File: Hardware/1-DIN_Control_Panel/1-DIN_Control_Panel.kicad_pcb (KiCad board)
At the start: 2 copper layers, 177.8 x 255.2 mm, 83 parts, among them J1 Selector Knob Connector, J2 Rotary Switch 1x7, J3 2x05 Molex Micro-Fit 3.0 43045, J4 UART Expansion, J5 SW - Aux Jump-Start, J6 SW - Battery Bypass, J7 SW - Master Power, J8 Pot/SW - Brightness, K1 FINDER-40.52, U1 CA56-12SEKWA, U2 CA56-12SEKWA, U3 LTV-847S, U4 LTV-847S, U5 MAX 6954 - SSOP, U6 MAX 6954 - SSOP, U7 LM324DR, U8 12V->5V Variable Boost Buck C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

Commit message: Organized schematic into two pages, begun PCB routing
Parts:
- removed C16, C17: DNP, Capacitor_SMD:C_0603_1608Metric_Pad1.08x0.95mm_HandSolder
- removed C18: 22µF, Capacitor_SMD:C_0603_1608Metric_Pad1.08x0.95mm_HandSolder
- removed R21: 0Ω or Bridge, Resistor_SMD:R_0603_1608Metric_Pad0.98x0.95mm_HandSolder
- removed TP10, TP11, TP12, TP13, TP14, TP3, TP4, TP5, TP6, TP7, TP8, TP9: TestPoint_Flag, TestPoint:TestPoint_Loop_D2.54mm_Drill1.5mm_Beaded
- added J10: 2x05 Molex Micro-Fit 3.0 43045, libraries:MOLEX_430450615, F.Cu at (169.4, 51.2)
- added J11: 2x05 Molex Micro-Fit 3.0 43045, libraries:MOLEX_430450615, B.Cu at (179.2, 151.8)
- added J12: Display LEDs, Connector_Molex:Molex_Micro-Fit_3.0_43045-0812_2x04_P3.00mm_Vertical, B.Cu at (91.2, 113.4)
- added J13: Mode LEDs, Connector_Molex:Molex_Micro-Fit_3.0_43045-0812_2x04_P3.00mm_Vertical, F.Cu at (82.2, 44.0)
- added J9: 2x05 Molex Micro-Fit 3.0 43045, libraries:MOLEX_430450615, B.Cu at (179.3, 123.1)
- added U10: XZFAVG10, libraries:XZFAVG10, F.Cu at (167.9, 147.1)
- added U11: MAX 6954 - SSOP, libraries:MAX6954-SSOP, B.Cu at (154.0, 134.8)
- added U12: LM324DR, Package_SO:SOIC-14_3.9x8.7mm_P1.27mm, F.Cu at (134.0, 64.2)
- added U13: 12V->5V Variable Boost Buck Converter, libraries:BoostBuck, F.Cu at (35.2, 87.2)
- added U9: XZFAVG10, libraries:XZFAVG10, F.Cu at (158.7, 147.1)
- A1: footprint Module:Arduino_Nano -> Module:Arduino_Nano_WithMountingHoles
- C1: value 47µF -> 22pF
- C11: value 100nF -> 10µF
- C12, C13: value 100nF -> DNP
- C14: value 100nF -> 22µF
- C15: value 10µF -> 100nF
- C2: footprint Capacitor_SMD:C_0603_1608Metric_Pad1.08x0.95mm_HandSolder -> Capacitor_SMD:C_1206_3216Metric_Pad1.33x1.80mm_HandSolder
- C7, C8: value 22pF -> 100nF
- J1: footprint libraries:Mystery_RJ45 -> Connector_Molex:Molex_Micro-Fit_3.0_43045-0812_2x04_P3.00mm_Vertical; moved to B.Cu
- J3, J4, R2, R3, R4, R5, R6, R7, R8: moved to B.Cu
- J8: footprint TerminalBlock:TerminalBlock_bornier-5_P5.08mm -> Connector_Molex:Molex_Micro-Fit_3.0_43650-0515_1x05_P3.00mm_Vertical
- R9: value 56kΩ -> 0Ω or Bridge
- RV1: footprint Buzzer_Beeper:Buzzer_12x9.5RM7.6 -> Potentiometer_THT:Potentiometer_Runtron_RM-065_Vertical
- TP1, TP2: footprint TestPoint:TestPoint_Loop_D2.54mm_Drill1.5mm_Beaded -> TestPoint:TestPoint_Pad_D4.0mm
- U1, U2: value CA56-12SEKWA -> XZFAVG10; footprint Display_7Segment:CA56-12SEKWA -> libraries:XZFAVG10
- U3, U4: value LTV-847S -> XZFAVG10; footprint Package_DIP:SMDIP-16_W9.53mm -> libraries:XZFAVG10
- U5, U6: value MAX 6954 - SSOP -> LTV-847S; footprint Package_SO:SSOP-44_5.3x12.8mm_P0.5mm -> Package_DIP:SMDIP-16_W9.53mm
- U7: value LM324DR -> XZFAVG10; footprint Package_SO:SOIC-14_3.9x8.7mm_P1.27mm -> libraries:XZFAVG10
- U8: value 12V->5V Variable Boost Buck Converter -> XZFAVG10; footprint libraries:BoostBuck -> libraries:XZFAVG10
- moved TP2 157.3 mm to (207.3, 149.4)
- moved TP1 157.0 mm to (207.3, 143.4)
- moved J4 149.3 mm to (181.1, 71.4), turned to -90 degrees
- moved J8 143.5 mm to (174.0, 85.2)
- moved U8 141.4 mm to (149.3, 147.1)
- moved C1 135.8 mm to (200.3, 134.7)
- moved U1 134.0 mm to (140.1, 122.8)
- moved C2 133.1 mm to (204.3, 126.5)
- moved C3 128.5 mm to (199.1, 128.6)
- moved C6 125.9 mm to (199.1, 131.2)
- moved U3 125.4 mm to (158.7, 122.8)
- moved U2 124.7 mm to (149.3, 122.8)
- moved U4 121.5 mm to (167.9, 122.8)
- moved R10 120.4 mm to (200.6, 137.3)
- moved C8 119.8 mm to (208.1, 48.8)
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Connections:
- net /12V_ON renamed /Back Board/12V_ON
- net /BATT_BYPASS renamed /Back Board/BATT_BYPASS
- net /BATT_RAW renamed /Back Board/BATT_RAW
- net /CONTACTOR_COIL renamed /Back Board/CONTACTOR_COIL
- net /MASTER_COMMON renamed /Back Board/MASTER_COMMON
- net /MASTER_OPEN renamed /Back Board/MASTER_OPEN
- net /RX-EXPANSION renamed /Back Board/RX-EXPANSION
- net /TX-EXPANSION renamed /Back Board/TX-EXPANSION
- net /VOLT_SOURCE_SELECT renamed /Back Board/VOLT_SOURCE_SELECT
- A1 pad 12: /Arduino_~{CS}_VOLT -> unconnected-(A1-D9-Pad12)
- A1 pad 13: /Arduino_~{CS}_AMP -> /Back Board/Arduino_~{CS}
- A1 pad 14: /Arduino_MOSI -> /Back Board/Arduino_MOSI
- A1 pad 15: /Arduino_MISO -> /Back Board/Arduino_MISO
- A1 pad 16: /Arduino_SCK -> /Back Board/Arduino_SCK
- A1 pad 19: /BRIGHTNESS_CONTROL -> /Back Board/BRIGHTNESS_CONTROL
- A1 pad 20: /VOLTAGE_SENSE -> /Back Board/VOLTAGE_SENSE
- A1 pad 21: /CURRENT_SENSE -> /Back Board/CURRENT_SENSE
- A1 pad 6: /MODE_LED_BRIGHTNESS -> /Back Board/MODE_LED_BRIGHTNESS
- A1 pad 7: /MODE_PWR_DETECT -> /Back Board/MODE_PWR_DETECT
- C1 pad 1: Net-(C1-Pad1) -> Net-(U11-OSC)
- C10 pad 1: /BRIGHTNESS_CONTROL -> /Back Board/SHUNT-
- C11 pad 1: /CURRENT_SENSE -> VCC
- C12 pad 1: /VOLTAGE_SENSE -> Net-(U12A--)
- C13 pad 1: /SHUNT+ -> Net-(U12A-+)
- C14 pad 1: /SHUNT- -> +5V
- C15 pad 1: VCC -> +5V
- C2 pad 1: Net-(C2-Pad1) -> +5V
- C3 pad 1: Net-(C1-Pad1) -> +5V
- C4 pad 1: Net-(C2-Pad1) -> /Back Board/VOLTAGE_SENSE
- C5 pad 1: Net-(C1-Pad1) -> /Back Board/BRIGHTNESS_CONTROL
- C6 pad 1: Net-(C2-Pad1) -> +5V
- C7 pad 1: Net-(U5-OSC) -> /Back Board/CURRENT_SENSE
- C8 pad 1: Net-(U6-OSC) -> /Back Board/VOLTAGE_SENSE
- C9 pad 1: /VOLTAGE_SENSE -> /Back Board/SHUNT+
- D1 pad 1: /MODE_1_LED -> Net-(D1-K)
- D2 pad 1: /MODE_2_LED -> Net-(D1-K)
- D3 pad 1: /MODE_3_LED -> Net-(D1-K)
- D4 pad 1: /MODE_4_LED -> Net-(D1-K)
- D5 pad 1: /MODE_5_LED -> Net-(D1-K)
- D6 pad 1: /MODE_6_LED -> Net-(D1-K)
- D7 pad 1: /MODE_7_LED -> Net-(D1-K)
- D9 pad 2: /SHUNT+ -> /Back Board/SHUNT+
- J1 pad 1: /MODE_1_OUT -> /Back Board/MODE_12V_OUT
- J1 pad 2: /MODE_2_OUT -> /Back Board/MODE_7_OUT
- J1 pad 3: /MODE_3_OUT -> /Back Board/MODE_6_OUT
- J1 pad 4: /MODE_4_OUT -> /Back Board/MODE_5_OUT
- J1 pad 5: /MODE_5_OUT -> /Back Board/MODE_4_OUT
- J1 pad 6: /MODE_6_OUT -> /Back Board/MODE_3_OUT
- J1 pad 7: /MODE_7_OUT -> /Back Board/MODE_2_OUT
- J1 pad 8: /MODE_12V_OUT -> /Back Board/MODE_1_OUT
- J2 pad 1: /MODE_1 -> /Back Board/MODE_1
- J2 pad 2: /MODE_2 -> /Back Board/MODE_2
- J2 pad 3: /MODE_3 -> /Back Board/MODE_3
- J2 pad 4: /MODE_4 -> /Back Board/MODE_4
- J2 pad 5: /MODE_5 -> /Back Board/MODE_5
- J2 pad 6: /MODE_6 -> /Back Board/MODE_6
- J2 pad 7: /MODE_7 -> /Back Board/MODE_7
- J2 pad 8: /MODE_12V -> /Back Board/MODE_12V
- J3 pad 2: /SHUNT+ -> /Back Board/SHUNT+
- J3 pad 3: /SHUNT- -> /Back Board/SHUNT-
- J6 pad 1: /SHUNT+ -> /Back Board/SHUNT+
- J8 pad 2: /BRIGHTNESS_CONTROL -> /Back Board/BRIGHTNESS_CONTROL
- R1 pad 2: /MODE_PWR_DETECT -> /Back Board/MODE_PWR_DETECT
- R10 pad 2: Net-(U6-ISET) -> Net-(U11-ISET)
- R12 pad 1: /VOLTAGE_SENSE -> /Back Board/VOLTAGE_SENSE
- R13 pad 2: /VOLTAGE_SENSE -> /Back Board/VOLTAGE_SENSE
- R14 pad 1: Net-(U7B--) -> Net-(U12B--)
- R15 pad 2: Net-(U7B--) -> Net-(U12B--)
- R16 pad 2: Net-(U7C--) -> Net-(U12C--)
- R17 pad 2: Net-(U7A--) -> Net-(U12A--)
- R18 pad 2: Net-(U7A-+) -> Net-(U12A-+)
- R19 pad 1: Net-(U7A--) -> Net-(U12A--)
- R19 pad 2: /CURRENT_SENSE -> /Back Board/CURRENT_SENSE
- R2 pad 1: Net-(R2-Pad1) -> Net-(J12-Pin_1)
- R20 pad 1: Net-(U7A-+) -> Net-(U12A-+)
- R3 pad 1: Net-(R2-Pad1) -> Net-(J12-Pin_2)
- R4 pad 1: Net-(R2-Pad1) -> Net-(J12-Pin_3)
- R5 pad 1: Net-(R2-Pad1) -> Net-(J12-Pin_4)
- R6 pad 1: Net-(R2-Pad1) -> Net-(J12-Pin_5)
- R7 pad 1: Net-(R2-Pad1) -> Net-(J12-Pin_6)
- R8 pad 1: Net-(R2-Pad1) -> Net-(J12-Pin_7)
- R9 pad 1: GND -> /Back Board/MODE_LED_BRIGHTNESS
- R9 pad 2: Net-(U5-ISET) -> Net-(J13-Pin_8)
- RV1 pad 2: Net-(U7C--) -> Net-(U12C--)
- TP1 pad 1: Net-(U5-P0) -> Net-(U11-BLINK)
- TP2 pad 1: Net-(U5-P1) -> Net-(U11-OSC_OUT)
- U1 pad 1: /DIGIT1_G2-N_ANODE -> /Front Board/6954_O10
- U1 pad 10: /DIGIT3_G2-N_ANODE -> /Front Board/6954_O2
- U1 pad 11: /DIGIT3_A-G1_ANODE -> /Front Board/6954_O4
- U1 pad 12: /F_CATHODE -> /Front Board/6954_O11
- U1 pad 2: /DIGIT2_G2-N_ANODE -> /Front Board/6954_O17
- U1 pad 3: /D_CATHODE -> /Front Board/6954_O13
- U1 pad 4: /C_CATHODE -> /Front Board/6954_O16
- U1 pad 5: /G_CATHODE -> /Front Board/6954_O18
- U1 pad 6: /E_CATHODE -> /Front Board/6954_O5
- U1 pad 7: /COLON_DP_ANODE -> /Front Board/6954_O6
- U1 pad 8: /DIGIT4_A-G1_ANODE -> /Front Board/6954_O8
- U1 pad 9: /DIGIT4_G2-N_ANODE -> /Front Board/6954_O14
- U2 pad 1: /DIGIT1_G2-N_ANODE -> /Front Board/6954_O10
- U2 pad 10: /DIGIT3_G2-N_ANODE -> /Front Board/6954_O0
- U2 pad 11: /DIGIT3_A-G1_ANODE -> /Front Board/6954_O2
- U2 pad 12: /F_CATHODE -> /Front Board/6954_O11
- U2 pad 2: /DIGIT2_G2-N_ANODE -> /Front Board/6954_O17
- U2 pad 3: /D_CATHODE -> /Front Board/6954_O13
- U2 pad 4: /C_CATHODE -> /Front Board/6954_O16
- U2 pad 5: /G_CATHODE -> /Front Board/6954_O18
- U2 pad 6: /E_CATHODE -> /Front Board/6954_O3
- U2 pad 7: /COLON_DP_ANODE -> /Front Board/6954_O6
- U2 pad 8: /DIGIT4_A-G1_ANODE -> /Front Board/6954_O8
- U2 pad 9: /DIGIT4_G2-N_ANODE -> /Front Board/6954_O14
- U3 pad 1: /MODE_1 -> /Front Board/6954_O10
- U3 pad 10: /MODE_4_LED -> /Front Board/6954_O2
- U3 pad 11: GND -> /Front Board/6954_O4
- U3 pad 12: /MODE_3_LED -> /Front Board/6954_O11
- U3 pad 13: GND -> /Front Board/6954_O15
- U3 pad 14: /MODE_2_LED -> /Front Board/6954_O1
- U3 pad 15: GND -> /Front Board/6954_O12
- U3 pad 16: /MODE_1_LED -> /Front Board/6954_O9
- U3 pad 2: /MODE_1_OUT -> /Front Board/6954_O17
- U3 pad 3: /MODE_2 -> /Front Board/6954_O13
- U3 pad 4: /MODE_2_OUT -> /Front Board/6954_O16
- U3 pad 5: /MODE_3 -> /Front Board/6954_O18
- U3 pad 6: /MODE_3_OUT -> /Front Board/6954_O5
- U3 pad 7: /MODE_4 -> /Front Board/6954_O6
- U3 pad 8: /MODE_4_OUT -> /Front Board/6954_O8
- U3 pad 9: GND -> /Front Board/6954_O14
- U4 pad 1: /MODE_5 -> /Front Board/6954_O10
- U4 pad 10: +5V -> /Front Board/6954_O0
- U4 pad 11: GND -> /Front Board/6954_O2
- U4 pad 12: /MODE_7_LED -> /Front Board/6954_O11
- U4 pad 13: GND -> /Front Board/6954_O15
- U4 pad 14: /MODE_6_LED -> /Front Board/6954_O5
- U4 pad 15: GND -> /Front Board/6954_O12
- U4 pad 16: /MODE_5_LED -> /Front Board/6954_O9
- U4 pad 2: /MODE_5_OUT -> /Front Board/6954_O17
- U4 pad 3: /MODE_6 -> /Front Board/6954_O13
- U4 pad 4: /MODE_6_OUT -> /Front Board/6954_O16
- U4 pad 5: /MODE_7 -> /Front Board/6954_O18
- U4 pad 6: /MODE_7_OUT -> /Front Board/6954_O3
- U4 pad 7: /MODE_12V_OUT -> /Front Board/6954_O6
- U4 pad 8: /MODE_12V -> /Front Board/6954_O8
- U4 pad 9: /MODE_PWR_DETECT -> /Front Board/6954_O14
- U5 pad 1: Net-(U5-P0) -> /Back Board/MODE_1
- U5 pad 10: /DIGIT2_G2-N_ANODE -> /Back Board/MODE_4_LED
- U5 pad 11: /DIGIT3_A-G1_ANODE -> GND
- U5 pad 12: /DIGIT3_G2-N_ANODE -> /Back Board/MODE_3_LED
- U5 pad 13: /DIGIT4_A-G1_ANODE -> GND
- U5 pad 14: /DIGIT4_G2-N_ANODE -> /Back Board/MODE_2_LED
- U5 pad 15: /COLON_DP_ANODE -> GND
- U5 pad 16: GND -> /Back Board/MODE_1_LED
- U5 pad 2: Net-(U5-P1) -> /Back Board/MODE_1_OUT
- U5 pad 3: /Arduino_~{CS}_VOLT -> /Back Board/MODE_2
- U5 pad 4: /Arduino_MISO -> /Back Board/MODE_2_OUT
- U5 pad 5: /Arduino_SCK -> /Back Board/MODE_3
- U5 pad 6: /Arduino_MOSI -> /Back Board/MODE_3_OUT
- U5 pad 7: /DIGIT1_A-G1_ANODE -> /Back Board/MODE_4
- U5 pad 8: /DIGIT1_G2-N_ANODE -> /Back Board/MODE_4_OUT
- U5 pad 9: /DIGIT2_A-G1_ANODE -> GND
- U6 pad 1: Net-(U6-P0) -> /Back Board/MODE_5
- U6 pad 10: /DIGIT2_G2-N_ANODE -> +5V
- U6 pad 11: /DIGIT3_A-G1_ANODE -> GND
- U6 pad 12: /DIGIT3_G2-N_ANODE -> /Back Board/MODE_7_LED
- U6 pad 13: /DIGIT4_A-G1_ANODE -> GND
- U6 pad 14: /DIGIT4_G2-N_ANODE -> /Back Board/MODE_6_LED
- U6 pad 15: /COLON_DP_ANODE -> GND
- U6 pad 16: GND -> /Back Board/MODE_5_LED
- U6 pad 2: Net-(U6-P1) -> /Back Board/MODE_5_OUT
- U6 pad 3: /Arduino_~{CS}_AMP -> /Back Board/MODE_6
- U6 pad 4: /Arduino_MISO -> /Back Board/MODE_6_OUT
- U6 pad 5: /Arduino_SCK -> /Back Board/MODE_7
- U6 pad 6: /Arduino_MOSI -> /Back Board/MODE_7_OUT
- U6 pad 7: /DIGIT1_A-G1_ANODE -> /Back Board/MODE_12V_OUT
- U6 pad 8: /DIGIT1_G2-N_ANODE -> /Back Board/MODE_12V
- U6 pad 9: /DIGIT2_A-G1_ANODE -> /Back Board/MODE_PWR_DETECT
- U7 pad 1: /CURRENT_SENSE -> /Front Board/6954_O10
- U7 pad 10: /SHUNT- -> /Front Board/6954_O0
- U7 pad 11: GND -> /Front Board/6954_O4
- U7 pad 12: unconnected-(U7D-+-Pad12) -> /Front Board/6954_O11
- U7 pad 13: unconnected-(U7D---Pad13) -> /Front Board/6954_O15
- U7 pad 14: unconnected-(U7-Pad14) -> /Front Board/6954_O2
- U7 pad 2: Net-(U7A--) -> /Front Board/6954_O17
- U7 pad 3: Net-(U7A-+) -> /Front Board/6954_O13
- U7 pad 4: +5V -> /Front Board/6954_O16
- U7 pad 5: /SHUNT+ -> /Front Board/6954_O18
- U7 pad 6: Net-(U7B--) -> /Front Board/6954_O5
- U7 pad 7: Net-(R14-Pad2) -> /Front Board/6954_O6
- U7 pad 8: Net-(R16-Pad1) -> /Front Board/6954_O8
- U7 pad 9: Net-(U7C--) -> /Front Board/6954_O14
- U8 pad 1: VCC -> /Front Board/6954_O10
- U8 pad 2: GND -> /Front Board/6954_O17
- U8 pad 3: +5V -> /Front Board/6954_O13
- U8 pad 4: GND -> /Front Board/6954_O16
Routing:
- net Net-(D1-K): track 0.00 -> 88.3 mm
- net Net-(D7-A): track 0.00 -> 41.6 mm, vias 0 -> 1
- net Net-(D1-A): track 0.00 -> 33.4 mm, vias 0 -> 1
- net Net-(J12-Pin_5): track 0.00 -> 32.8 mm
- net Net-(J12-Pin_1): track 0.00 -> 32.8 mm
- net Net-(D6-A): track 0.00 -> 31.1 mm, vias 0 -> 1
- net Net-(D2-A): track 0.00 -> 28.2 mm, vias 0 -> 1
- net Net-(J12-Pin_2): track 0.00 -> 25.3 mm
- net Net-(J12-Pin_6): track 0.00 -> 24.9 mm
- net Net-(D5-A): track 0.00 -> 21.5 mm, vias 0 -> 1
- net Net-(R14-Pad2): track 0.00 -> 18.5 mm, vias 0 -> 2
- net Net-(R15-Pad1): track 0.00 -> 18.1 mm, vias 0 -> 2
- net Net-(J12-Pin_3): track 0.00 -> 17.4 mm
- net Net-(D3-A): track 0.00 -> 15.3 mm, vias 0 -> 1
- net Net-(J12-Pin_7): track 0.00 -> 14.3 mm
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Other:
- board size 177.8 x 255.2 mm -> 374.9 x 296.6 mm

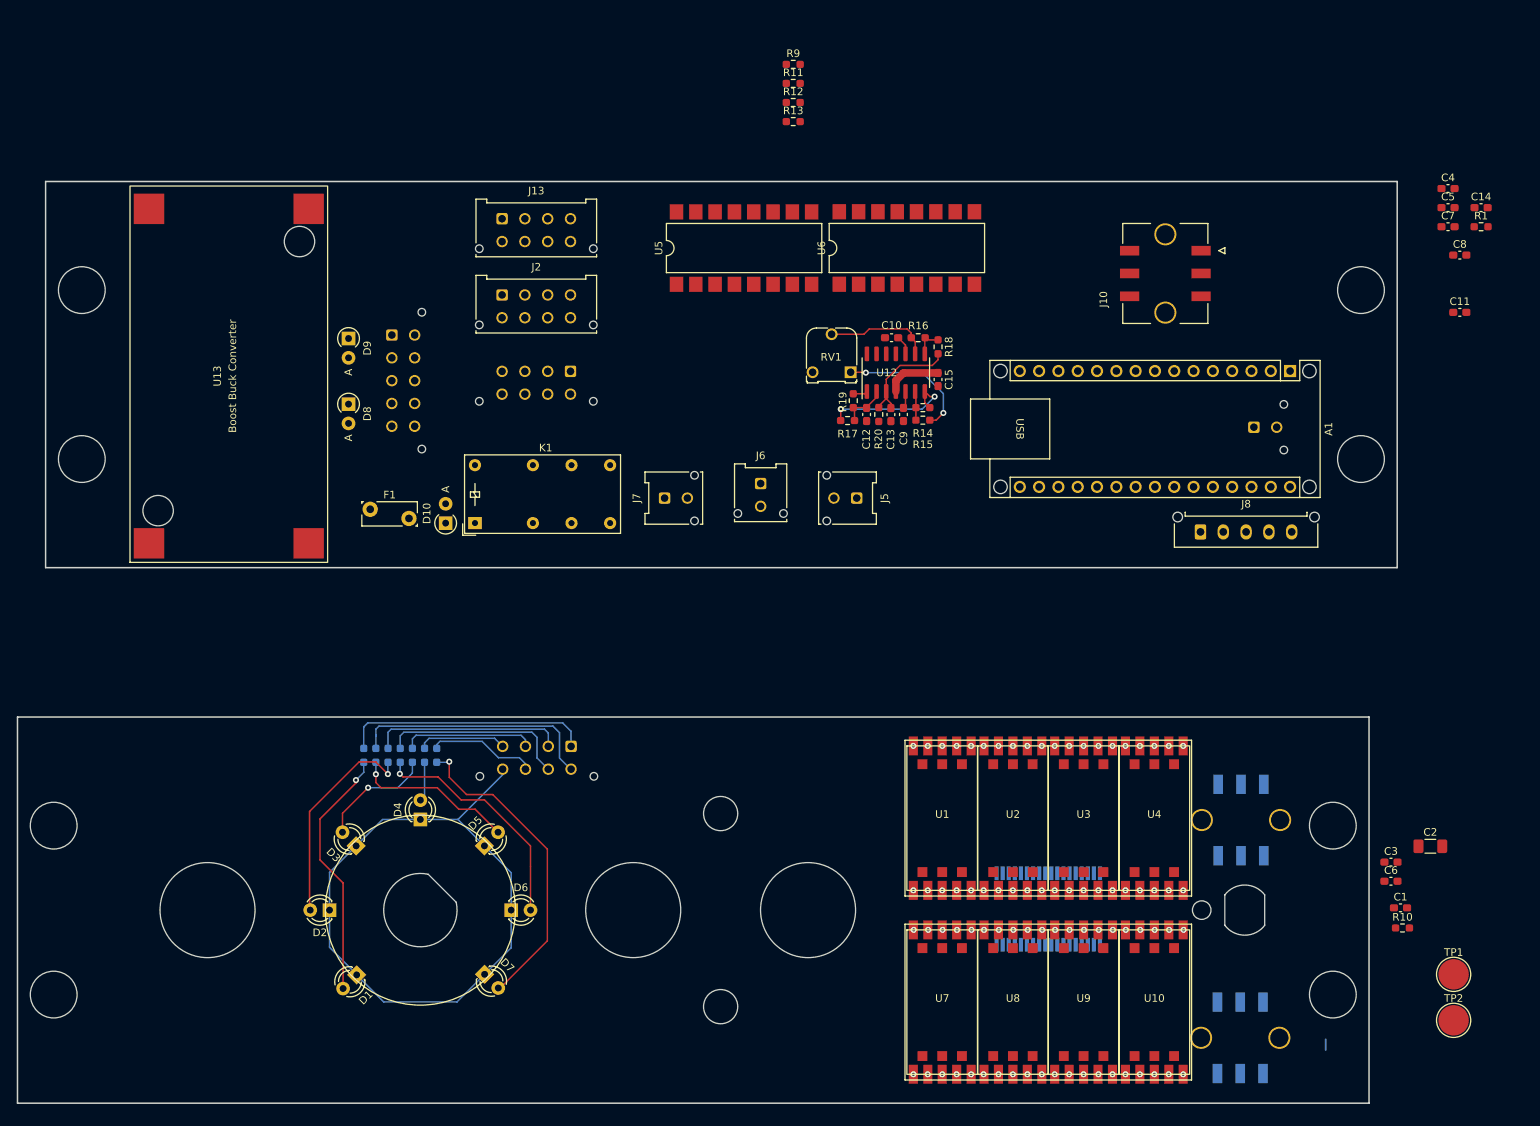
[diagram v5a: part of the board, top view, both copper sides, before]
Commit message: Finished routing of rear board
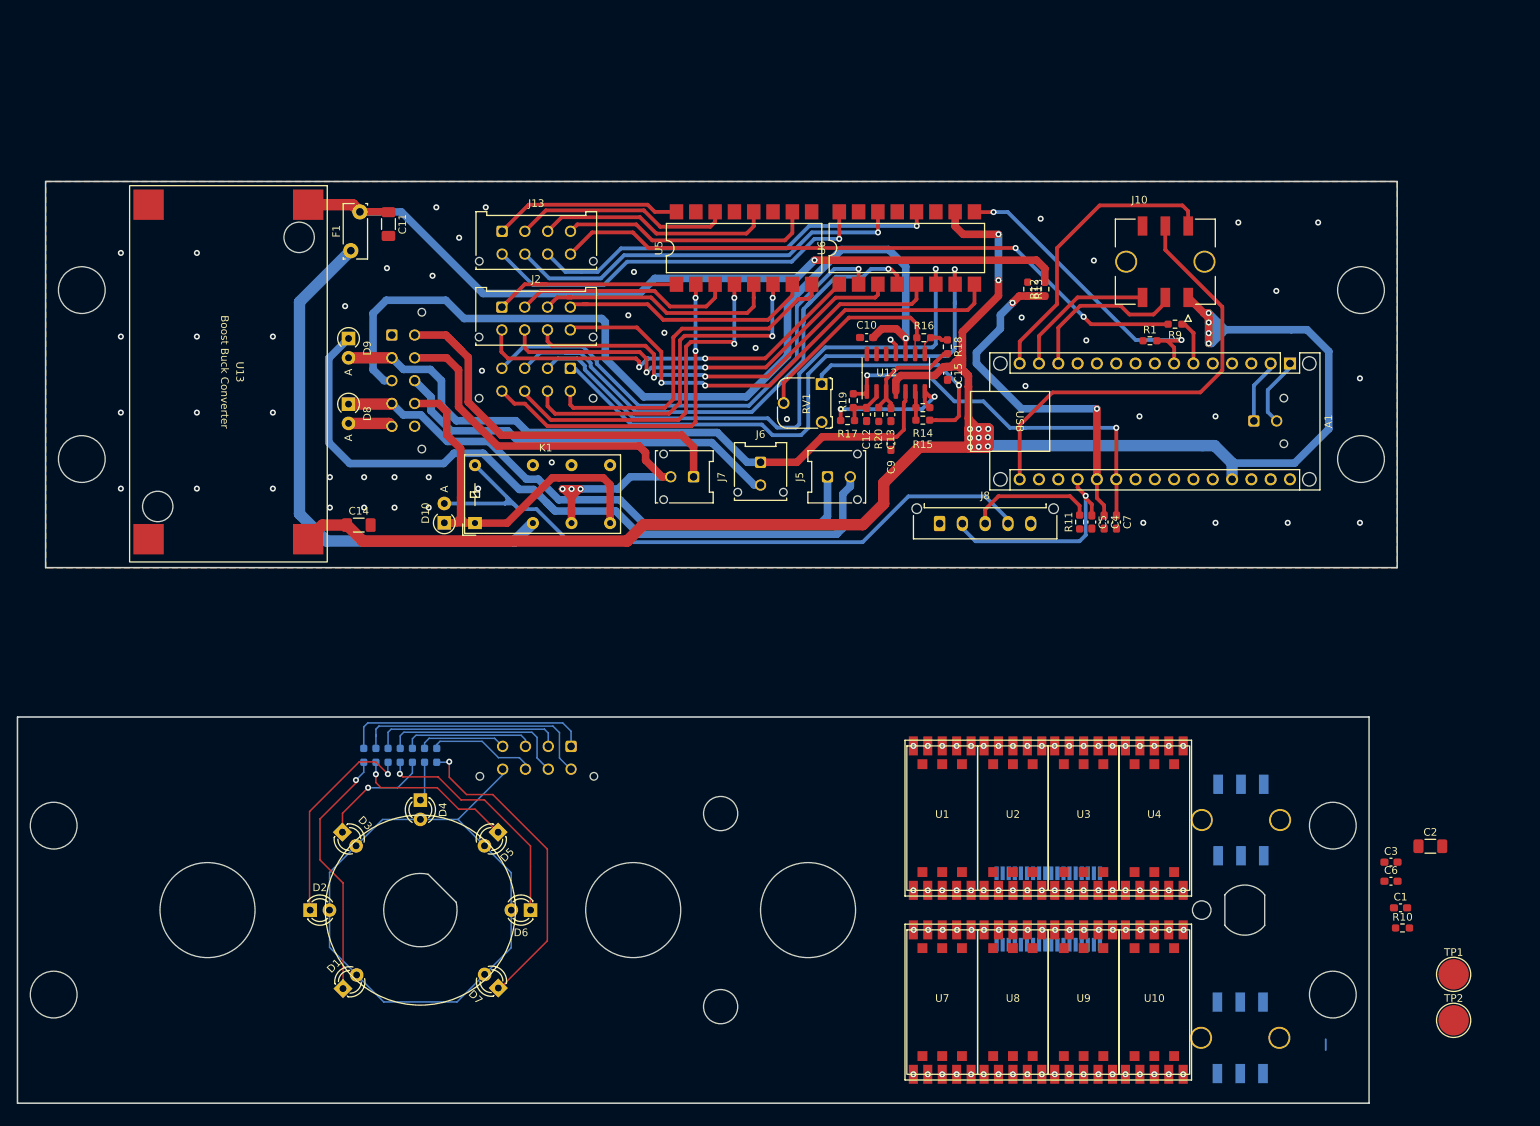
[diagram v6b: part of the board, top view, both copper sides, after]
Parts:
- removed C8: 100nF, Capacitor_SMD:C_0603_1608Metric_Pad1.08x0.95mm_HandSolder
- C11, C14: footprint Capacitor_SMD:C_0603_1608Metric_Pad1.08x0.95mm_HandSolder -> Capacitor_SMD:C_1206_3216Metric_Pad1.33x1.80mm_HandSolder
- moved C14 153.4 mm to (63.3, 84.3)
- moved C11 141.4 mm to (67.2, 44.7), turned to -90 degrees
- moved R11 68.9 mm to (158.1, 83.9), turned to 90 degrees
- moved C4 63.0 mm to (161.3, 83.9), turned to -90 degrees
- moved C5 62.5 mm to (159.7, 83.9), turned to -90 degrees
- moved R9 60.8 mm to (170.7, 57.9), turned to 180 degrees
- moved C7 58.4 mm to (163.0, 83.9), turned to -90 degrees
- moved U13 50.6 mm to (57.2, 41.6), turned to -90 degrees
- moved R1 46.1 mm to (167.4, 60.0)
- moved R12 41.2 mm to (153.6, 53.3), turned to 90 degrees
- moved R13 37.9 mm to (151.3, 53.3), turned to -90 degrees
- moved J8 34.3 mm to (139.7, 84.1)
- moved F1 34.1 mm to (62.2, 48.2), turned to 90 degrees
- moved J5 4.75 mm to (125.0, 77.9), turned to 90 degrees
- moved J7 4.73 mm to (107.3, 78.0), turned to -90 degrees
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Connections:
- D2 pad 1: Net-(D1-K) -> Net-(D2-K)
- D2 pad 2: Net-(D2-A) -> Net-(D1-A)
- D3 pad 1: Net-(D1-K) -> Net-(D3-K)
- D3 pad 2: Net-(D3-A) -> Net-(D1-A)
- D4 pad 1: Net-(D1-K) -> Net-(D4-K)
- D4 pad 2: Net-(D4-A) -> Net-(D1-A)
- D5 pad 1: Net-(D1-K) -> Net-(D5-K)
- D5 pad 2: Net-(D5-A) -> Net-(D1-A)
- D6 pad 1: Net-(D1-K) -> Net-(D6-K)
- D6 pad 2: Net-(D6-A) -> Net-(D1-A)
- D7 pad 1: Net-(D1-K) -> Net-(D7-K)
- D7 pad 2: Net-(D7-A) -> Net-(D1-A)
- J12 pad 8: Net-(D1-K) -> Net-(D1-A)
- R2 pad 2: Net-(D1-A) -> Net-(D1-K)
- R3 pad 2: Net-(D2-A) -> Net-(D2-K)
- R4 pad 2: Net-(D3-A) -> Net-(D3-K)
- R5 pad 2: Net-(D4-A) -> Net-(D4-K)
- R6 pad 2: Net-(D5-A) -> Net-(D5-K)
- R7 pad 2: Net-(D6-A) -> Net-(D6-K)
- R8 pad 2: Net-(D7-A) -> Net-(D7-K)
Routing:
- net +5V: track 7.40 -> 289.5 mm, vias 0 -> 15
- net /Back Board/SHUNT-: track 2.53 -> 119.1 mm, vias 0 -> 1
- net VCC: track 0.00 -> 109.1 mm, vias 0 -> 1
- net Net-(D9-K): track 0.00 -> 97.2 mm
- net /Back Board/VOLT_SOURCE_SELECT: track 0.00 -> 90.5 mm
- net /Back Board/SHUNT+: track 2.27 -> 87.6 mm
- net Net-(J13-Pin_8): track 0.00 -> 84.9 mm, vias 0 -> 2
- net /Back Board/MODE_7_OUT: track 0.00 -> 76.1 mm, vias 0 -> 1
- net /Back Board/MODE_12V_OUT: track 0.00 -> 75.9 mm, vias 0 -> 1
- net /Back Board/CONTACTOR_COIL: track 0.00 -> 75.2 mm
- net /Back Board/MODE_6_OUT: track 0.00 -> 70.9 mm, vias 0 -> 1
- net Net-(F1-Pad1): track 0.00 -> 70.6 mm
- net /Back Board/MASTER_COMMON: track 0.00 -> 68.6 mm, vias 0 -> 3
- net /Back Board/MODE_12V: track 0.00 -> 65.9 mm, vias 0 -> 2
- net /Back Board/MODE_5_OUT: track 0.00 -> 65.0 mm, vias 0 -> 1
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- added copper zone on B.Cu, net GND
- added copper zone on F.Cu, net GND

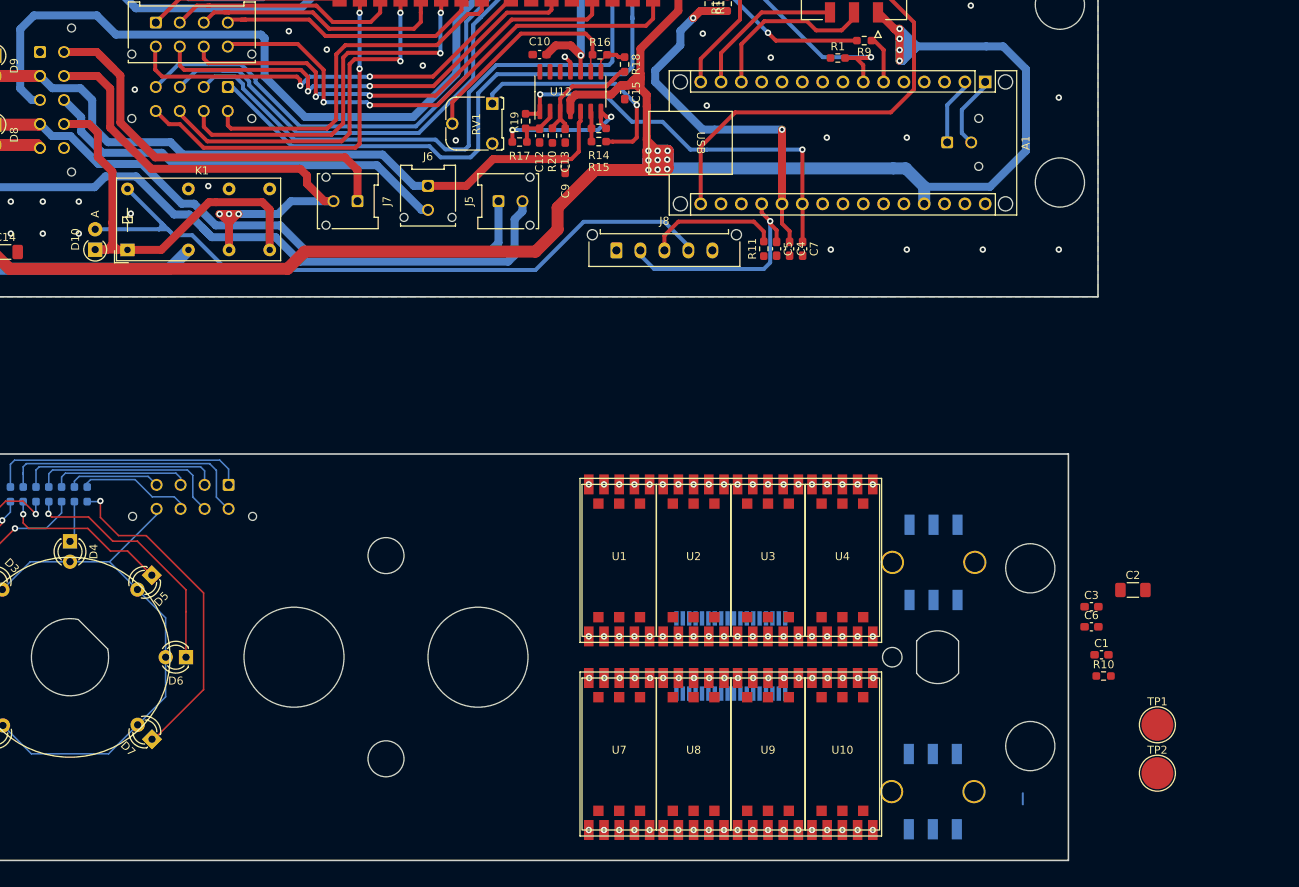
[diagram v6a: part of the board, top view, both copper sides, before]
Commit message: Routed most of the front panel
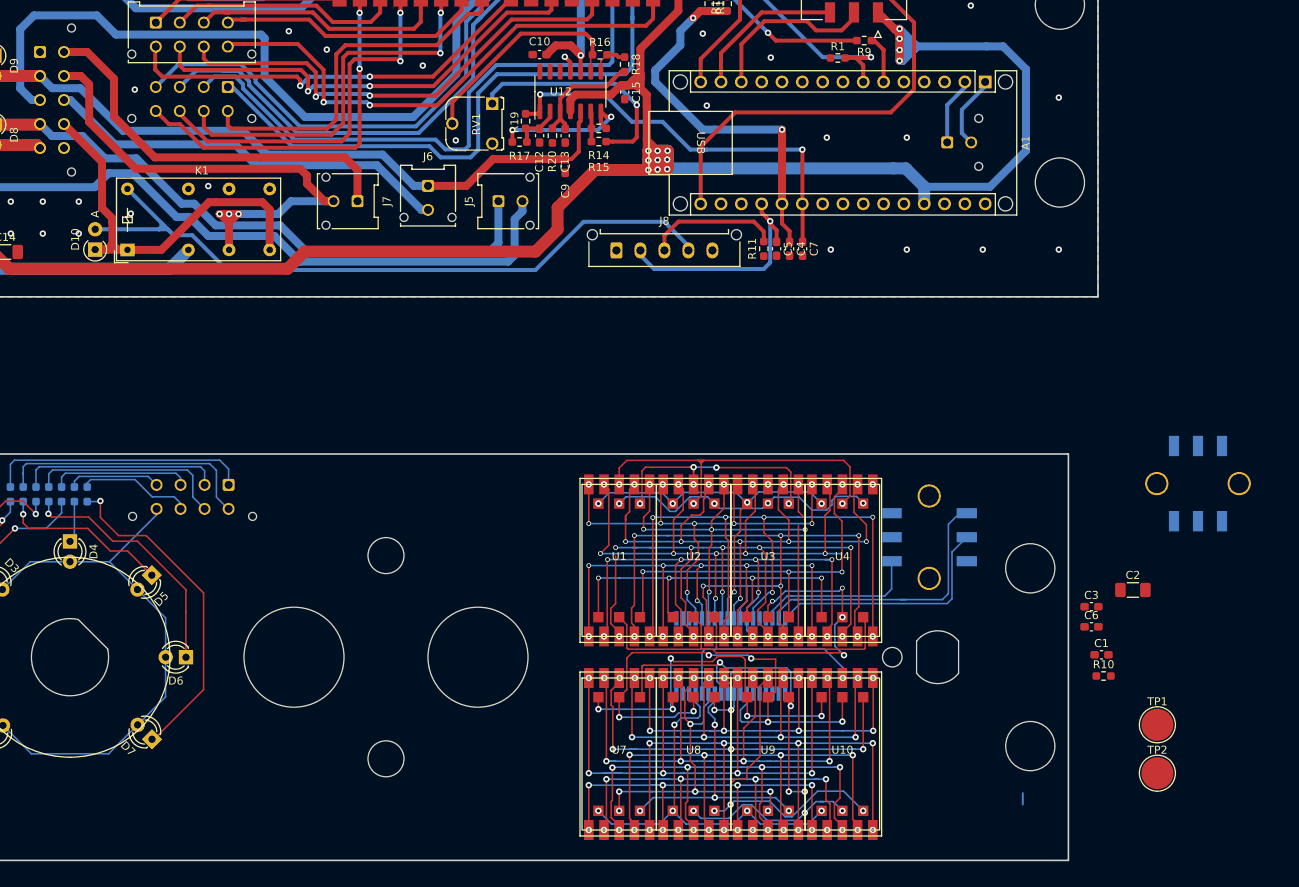
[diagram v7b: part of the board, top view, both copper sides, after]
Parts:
- moved J9 34.5 mm to (212.4, 113.2)
- moved J11 31.8 mm to (178.8, 120.0), turned to 90 degrees
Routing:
- net /Front Board/6954_O18: track 0.00 -> 172.1 mm, vias 8 -> 17
- net /Front Board/6954_O16: track 0.00 -> 155.4 mm, vias 8 -> 17
- net /Front Board/6954_O12: track 0.00 -> 149.9 mm, vias 8 -> 18
- net /Front Board/6954_O13: track 0.00 -> 149.0 mm, vias 8 -> 18
- net /Front Board/6954_O9: track 0.00 -> 139.8 mm, vias 8 -> 17
- net /Front Board/6954_O15: track 0.00 -> 134.8 mm, vias 8 -> 18
- net /Front Board/6954_O17: track 0.00 -> 127.0 mm, vias 8 -> 17
- net /Front Board/6954_O10: track 0.14 -> 122.8 mm, vias 8 -> 18
- net /Front Board/6954_O0: track 0.00 -> 109.6 mm, vias 1 -> 9
- net /Front Board/6954_O11: track 0.00 -> 105.9 mm, vias 8 -> 16
- net /Front Board/6954_O4: track 0.00 -> 105.8 mm, vias 1 -> 12
- net /Front Board/6954_O6: track 0.00 -> 103.6 mm, vias 1 -> 11
- net /Front Board/6954_O8: track 0.00 -> 97.7 mm, vias 0 -> 9
- net /Front Board/6954_O2: track 0.00 -> 94.9 mm, vias 1 -> 10
- net /Front Board/6954_O14: track 0.00 -> 94.2 mm, vias 0 -> 10
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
